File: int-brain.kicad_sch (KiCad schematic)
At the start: 62 parts, among them J1 Top, J10 2MB, J11 1MB, J12 1MA, J13 1MA_ENC, J14 1MB_ENC, J15 2MA_ENC, J16 MPU9250, J17 VBATT_SELECT, J2 Bottom, J3 PWR, J4 PWR, J5 USB_A, J6 2MB_ENC, J7 I2C0, J8 UART0, J9 2MA, SW1 SW_Push, U1 PCA9635, U13 AMS1117-3.3, U2 ESP32-DevKitC

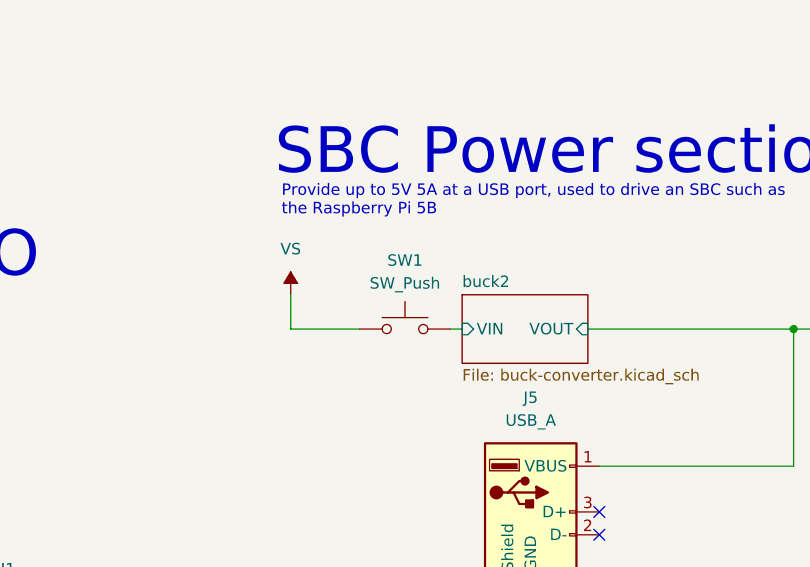
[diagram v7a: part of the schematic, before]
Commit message: footprint updates
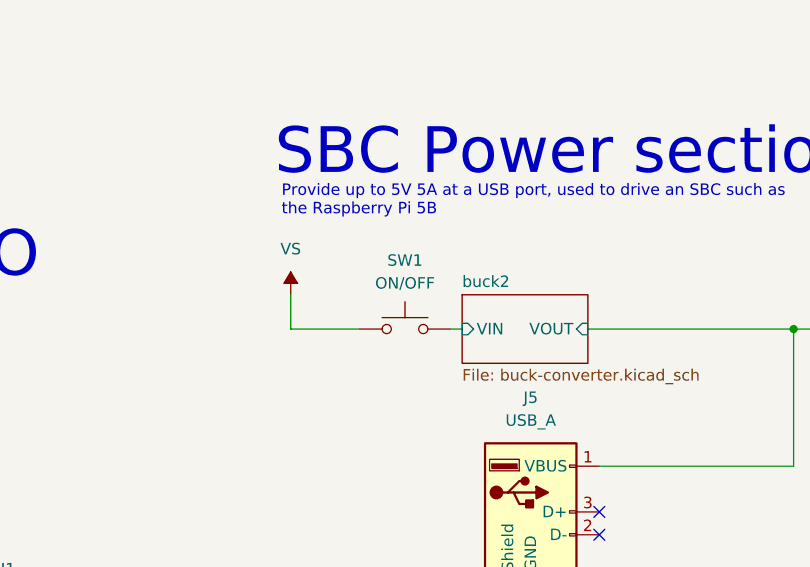
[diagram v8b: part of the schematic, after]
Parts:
- C1: footprint Capacitor_SMD:C_0603_1608Metric_Pad1.08x0.95mm_HandSolder -> Capacitor_SMD:C_0805_2012Metric_Pad1.18x1.45mm_HandSolder
- SW1: value SW_Push -> ON/OFF
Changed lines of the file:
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@@
 			)
 		)
-		(property "Footprint" "Capacitor_SMD:C_0603_1608Metric_Pad1.08x0.95mm_HandSolder"
+		(property "Footprint" "Capacitor_SMD:C_0805_2012Metric_Pad1.18x1.45mm_HandSolder"
 			(at 171.45 341.3252 0)
 			(effects
@@
 			)
 		)
-		(property "Description" "Generic connector, single row, 01x19, script generated"
+		(property "Description" "Female jumper header"
 			(at 45.72 247.65 0)
 			(effects
@@
 			)
 		)
-		(property "Value" "SW_Push"
+		(property "Value" "ON/OFF"
 			(at 250.19 477.52 0)
 			(effects
@@
 			)
 		)
-		(property "Description" "Generic connector, single row, 01x19, script generated"
+		(property "Description" "Female jumper header"
 			(at 45.72 193.04 0)
 			(effects
@@
 			)
 		)
-		(property "Description" ""
+		(property "Description" "Female jumper header"
 			(at 336.55 474.98 0)
 			(effects
